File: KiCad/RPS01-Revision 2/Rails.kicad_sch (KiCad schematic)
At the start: 91 parts, among them J200 Power In, J201 Power Out, J202 Header Pins, Q200 BSC009NE2LS5IATMA1 A (TG2)(1A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, Q201 BSC009NE2LS5IATMA1 D (TG1)(2B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, Q202 BSC009NE2LS5IATMA1 C (BG1)(2A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, Q203 BSC009NE2LS5IATMA1 B (BG2)(1B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, U11 LM340MPX-5.0/NOPB, U200 LTC3780EUH-TRPBF, U21 LM340MPX-5.0/NOPB

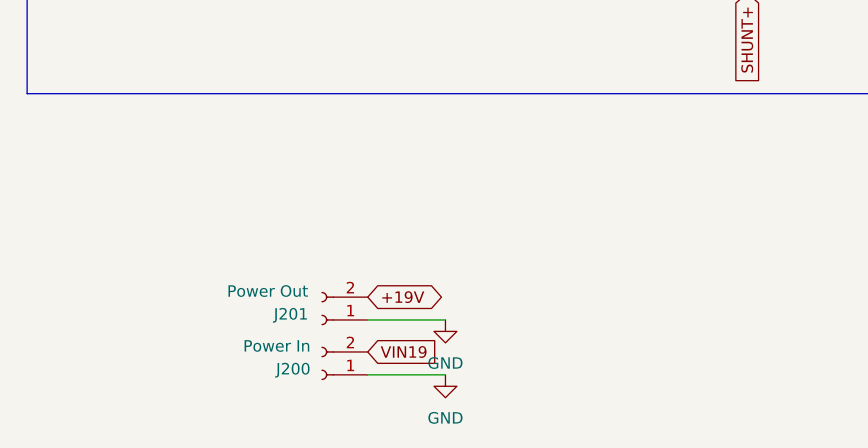
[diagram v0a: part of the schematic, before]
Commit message: Updated some MCU
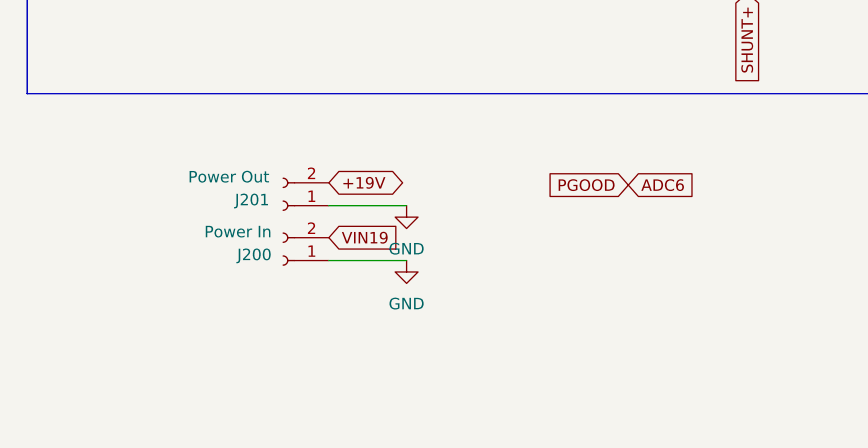
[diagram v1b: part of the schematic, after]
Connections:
- net PGOOD renamed ADC6
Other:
- moved on the sheet: J200, J201
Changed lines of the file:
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@@
     (stroke (width 0) (type default))
   )
-  (wire (pts (xy 289.306 390.906) (xy 297.942 390.906))
+  (wire (pts (xy 284.988 378.206) (xy 293.624 378.206))
     (stroke (width 0) (type default))
   )
@@
     (stroke (width 0) (type default))
   )
-  (wire (pts (xy 289.306 384.81) (xy 297.942 384.81))
+  (wire (pts (xy 284.988 372.11) (xy 293.624 372.11))
     (stroke (width 0) (type default))
   )
@@
     )
   )
-  (global_label "VIN19" (shape input) (at 289.306 388.366 0) (fields_autoplaced)
+  (global_label "VIN19" (shape input) (at 284.988 375.666 0) (fields_autoplaced)
     (effects (font (size 1.27 1.27)) (justify left))
-    (property "Intersheetrefs" "${INTERSHEET_REFS}" (at 297.6547 388.366 0)
+    (property "Intersheetrefs" "${INTERSHEET_REFS}" (at 293.3367 375.666 0)
       (effects (font (size 1.27 1.27)) (justify left) hide)
     )
@@
     )
   )
+  (global_label "PGOOD" (shape input) (at 318.262 369.824 180) (fields_autoplaced)
+    (effects (font (size 1.27 1.27)) (justify right))
+    (property "Intersheetrefs" "${INTERSHEET_REFS}" (at 308.8852 369.824 0)
+      (effects (font (size 1.27 1.27)) (justify right) hide)
+    )
+  )
   (global_label "BOOST2" (shape input) (at 429.514 330.708 180) (fields_autoplaced)
     (effects (font (size 1.27 1.27)) (justify right))
@@
     )
   )
+  (global_label "ADC6" (shape input) (at 318.262 369.824 0) (fields_autoplaced)
+    (effects (font (size 1.27 1.27)) (justify left))
+    (property "Intersheetrefs" "${INTERSHEET_REFS}" (at 326.0059 369.824 0)
+      (effects (font (size 1.27 1.27)) (justify left) hide)
+    )
+  )
   (global_label "VOS+" (shape input) (at 518.922 218.694 180) (fields_autoplaced)
     (effects (font (size 1.27 1.27)) (justify right))
@@
     )
   )
-  (global_label "+19V" (shape bidirectional) (at 289.306 382.27 0) (fields_autoplaced)
+  (global_label "+19V" (shape bidirectional) (at 284.988 369.57 0) (fields_autoplaced)
     (effects (font (size 1.27 1.27)) (justify left))
-    (property "Intersheetrefs" "${INTERSHEET_REFS}" (at 298.4031 382.27 0)
+    (property "Intersheetrefs" "${INTERSHEET_REFS}" (at 294.0851 369.57 0)
       (effects (font (size 1.27 1.27)) (justify left) hide)
     )
@@
     )
   )
-  (symbol (lib_id "power:GND") (at 297.942 390.906 0) (unit 1)
+  (symbol (lib_id "power:GND") (at 293.624 378.206 0) (unit 1)
     (in_bom yes) (on_board yes) (dnp no) (fields_autoplaced)
-    (property "Reference" "#PWR0112" (at 297.942 397.256 0)
+    (property "Reference" "#PWR0112" (at 293.624 384.556 0)
       (effects (font (size 1.27 1.27)) hide)
     )
-    (property "Value" "GND" (at 297.942 395.732 0)
+    (property "Value" "GND" (at 293.624 383.032 0)
       (effects (font (size 1.27 1.27)))
     )
-    (property "Footprint" "" (at 297.942 390.906 0)
+    (property "Footprint" "" (at 293.624 378.206 0)
       (effects (font (size 1.27 1.27)) hide)
     )
-    (property "Datasheet" "" (at 297.942 390.906 0)
+    (property "Datasheet" "" (at 293.624 378.206 0)
       (effects (font (size 1.27 1.27)) hide)
     )
@@
     )
   )
-  (symbol (lib_id "power:GND") (at 297.942 384.81 0) (unit 1)
+  (symbol (lib_id "power:GND") (at 293.624 372.11 0) (unit 1)
     (in_bom yes) (on_board yes) (dnp no) (fields_autoplaced)
-    (property "Reference" "#PWR0111" (at 297.942 391.16 0)
+    (property "Reference" "#PWR0111" (at 293.624 378.46 0)
       (effects (font (size 1.27 1.27)) hide)
     )
-    (property "Value" "GND" (at 297.942 389.636 0)
+    (property "Value" "GND" (at 293.624 376.936 0)
       (effects (font (size 1.27 1.27)))
     )
-    (property "Footprint" "" (at 297.942 384.81 0)
+    (property "Footprint" "" (at 293.624 372.11 0)
       (effects (font (size 1.27 1.27)) hide)
     )
-    (property "Datasheet" "" (at 297.942 384.81 0)
+    (property "Datasheet" "" (at 293.624 372.11 0)
       (effects (font (size 1.27 1.27)) hide)
     )
@@
     )
   )
-  (symbol (lib_id "Connector:Conn_01x02_Socket") (at 284.226 390.906 180) (unit 1)
+  (symbol (lib_id "Connector:Conn_01x02_Socket") (at 279.908 378.206 180) (unit 1)
     (in_bom yes) (on_board yes) (dnp no) (fields_autoplaced)
-    (property "Reference" "J200" (at 282.956 390.271 0)
+    (property "Reference" "J200" (at 278.638 377.571 0)
       (effects (font (size 1.27 1.27)) (justify left))
     )
-    (property "Value" "Power In" (at 282.956 387.731 0)
+    (property "Value" "Power In" (at 278.638 375.031 0)
       (effects (font (size 1.27 1.27)) (justify left))
     )
-    (property "Footprint" "Connector_AMASS:AMASS_XT30U-M_1x02_P5.0mm_Vertical" (at 284.226 390.906 0)
+    (property "Footprint" "Connector_AMASS:AMASS_XT30U-M_1x02_P5.0mm_Vertical" (at 279.908 378.206 0)
       (effects (font (size 1.27 1.27)) hide)
     )
-    (property "Datasheet" "~" (at 284.226 390.906 0)
+    (property "Datasheet" "~" (at 279.908 378.206 0)
       (effects (font (size 1.27 1.27)) hide)
     )
@@
     )
   )
-  (symbol (lib_id "Connector:Conn_01x02_Socket") (at 284.226 384.81 180) (unit 1)
+  (symbol (lib_id "Connector:Conn_01x02_Socket") (at 279.908 372.11 180) (unit 1)
     (in_bom yes) (on_board yes) (dnp no) (fields_autoplaced)
-    (property "Reference" "J201" (at 282.702 384.175 0)
+    (property "Reference" "J201" (at 278.384 371.475 0)
       (effects (font (size 1.27 1.27)) (justify left))
     )
-    (property "Value" "Power Out" (at 282.702 381.635 0)
+    (property "Value" "Power Out" (at 278.384 368.935 0)
       (effects (font (size 1.27 1.27)) (justify left))
     )
-    (property "Footprint" "Connector_AMASS:AMASS_XT30U-F_1x02_P5.0mm_Vertical" (at 284.226 384.81 0)
+    (property "Footprint" "Connector_AMASS:AMASS_XT30U-F_1x02_P5.0mm_Vertical" (at 279.908 372.11 0)
       (effects (font (size 1.27 1.27)) hide)
     )
-    (property "Datasheet" "~" (at 284.226 384.81 0)
+    (property "Datasheet" "~" (at 279.908 372.11 0)
       (effects (font (size 1.27 1.27)) hide)
     )

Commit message: Changed Schematic Refs (pg 2 to 4)
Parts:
- renumbered C216 to C10, C212 to C11, C210 to C12, C200 to C13, C205 to C14, C203 to C15, C218 to C16, C201 to C17, C213 to C18, C215 to C19, C209 to C20, C211 to C21, C214 to C22, C208 to C23, C217 to C24, C207 to C25, C202 to C7, C204 to C8, C206 to C9, D5 to D1, D205 to D10, D6 to D2, D2 to D3, D1 to D4, D204 to D5, D200 to D6, D203 to D7, D201 to D8, D202 to D9, J202 to J13, J201 to J14, J200 to J15, L200 to L2, Q200 to Q1, Q203 to Q2, Q201 to Q3, Q202 to Q4, R208 to R10, R205 to R11, R202 to R12, R204 to R13, R203 to R14, R213 to R15, R201 to R16, R210 to R17, R200 to R18, R214 to R19, R209 to R20, R211 to R21, R207 to R22, R206 to R23, R212 to R9, U21 to U12, U11 to U13, U200 to U16

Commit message: Reduced the References for Peter
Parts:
- renumbered C7 to C15, C8 to C16, C9 to C19, C10 to C20, C11 to C22, C12 to C23, C13 to C24, C14 to C25, C15 to C26, C16 to C27, C17 to C28, C18 to C29, C19 to C32, C20 to C33, C21 to C34, C22 to C35, C23 to C36, C24 to C37, C25 to C38, D9 to D10, D10 to D11, D6 to D7, D7 to D8, D8 to D9, F_3LOGIC1 to F1, F_5LOGIC1 to F2, F_5VB1 to F3, F_12VB1 to F4, R9 to R11, R10 to R12, R11 to R13, R12 to R14, R13 to R15, R14 to R17, R15 to R18, R16 to R19, R17 to R20, R18 to R21, R3_5VB1 to R23, R4_5VB1 to R24, R19 to R25, R20 to R26, R21 to R27, R22 to R28, R23 to R31, R3_12VB1 to R32, R4_12VB1 to R33

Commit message: Completed Schematic
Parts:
- removed J14: Power Out, Connector_AMASS:AMASS_XT30U-F_1x02_P5.0mm_Vertical, symbol Connector:Conn_01x02_Socket
- removed J15: Power In, Connector_AMASS:AMASS_XT30U-M_1x02_P5.0mm_Vertical, symbol Connector:Conn_01x02_Socket
- added F5: 5, Mechatronics Fuses:0154Series_LTF, symbol Device:Fuse_Small
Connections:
- net +19V: now also F5.2; no longer C34.2, C36.2, C38.2, R31.1
- new net: C34.2, C36.2, C38.2, F5.1, R31.1

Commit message: Updates
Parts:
- D7: value B0540W -> S_DIODE_10A; footprint Mechatronic Footprints:CR_SMA_320-340AE_DIO -> Diode_SMD:D_PowerDI-5
- D8: value 1N5819HW -> S_DIODE_10A; footprint Mechatronic Footprints:CR_SMA_320-340AE_DIO -> Diode_SMD:D_PowerDI-5
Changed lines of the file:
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@@
       (effects (font (size 1.27 1.27)) (justify left))
     )
-    (property "Value" "B0540W" (at 317.246 338.074 90)
-      (effects (font (size 1.27 1.27)) (justify left))
-    )
-    (property "Footprint" "Mechatronic Footprints:CR_SMA_320-340AE_DIO" (at 327.152 339.598 0)
+    (property "Value" "S_DIODE_10A" (at 312.42 339.852 90)
+      (effects (font (size 1.27 1.27)) (justify left))
+    )
+    (property "Footprint" "Diode_SMD:D_PowerDI-5" (at 327.152 339.598 0)
       (effects (font (size 1.27 1.27)) hide)
     )
@@
       (effects (font (size 1.27 1.27)))
     )
-    (property "Value" "1N5819HW" (at 343.408 307.848 0)
-      (effects (font (size 1.27 1.27)))
-    )
-    (property "Footprint" "Mechatronic Footprints:CR_SMA_320-340AE_DIO" (at 341.63 310.388 0)
-      (effects (font (size 1.27 1.27)) hide)
-    )
+    (property "Value" "S_DIODE_10A" (at 345.694 313.944 0)
+      (effects (font (size 1.27 1.27)))
+    )
+    (property "Footprint" "Diode_SMD:D_PowerDI-5" (at 341.63 310.388 0)
+      (effects (font (size 1.27 1.27)) hide)
+    )

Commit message: Update
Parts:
- removed R28: 10, Resistor_SMD:R_1206_3216Metric_Pad1.30x1.75mm_HandSolder, symbol Device:R_Small_US
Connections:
- net VIN19 is gone; now on net +BATT2: C24.2, C26.2, C28.2, C35.1, J13.2 (Pin_2), Q1.5, Q1.6, Q1.7, Q1.8, R12.1
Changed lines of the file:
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@@
     (stroke (width 0) (type default))
   )
-  (wire (pts (xy 458.47 215.138) (xy 463.55 215.138))
-    (stroke (width 0) (type default))
-  )
   (wire (pts (xy 292.862 228.092) (xy 294.386 228.092))
     (stroke (width 0) (type default))
@@
     (stroke (width 0) (type default))
   )
-  (wire (pts (xy 468.63 215.138) (xy 471.932 215.138))
+  (wire (pts (xy 458.47 215.138) (xy 471.932 215.138))
     (stroke (width 0) (type default))
   )
@@
         )
       )
-    )
-  )
-  (symbol (lib_id "Device:R_Small_US") (at 466.09 215.138 270) (unit 1)
-    (in_bom yes) (on_board yes) (dnp no)
-    (property "Reference" "R28" (at 466.344 218.186 90)
-      (effects (font (size 1.27 1.27)))
-    )
-    (property "Value" "10" (at 466.471 220.599 90)
-      (effects (font (size 1.27 1.27)))
-    )
-    (property "Footprint" "Resistor_SMD:R_1206_3216Metric_Pad1.30x1.75mm_HandSolder" (at 466.09 215.138 0)
-      (effects (font (size 1.27 1.27)) hide)
-    )
-    (property "Datasheet" "~" (at 466.09 215.138 0)
-      (effects (font (size 1.27 1.27)) hide)
-    )
-    (pin "1")
-    (pin "2")
-    (instances
-      (project "rps01"
-        (path "/14930f15-c0a0-4b55-93e6-b112548415f6/6ed54b0f-f89c-4a82-b1ab-c92c0c126d05"
-          (reference "R28") (unit 1)
-        )
-      )
-      (project "KENESP32LTC370TEST"
-        (path "/5e9cfb74-656a-48c0-8f94-6c53cb1501bf"
-          (reference "R207") (unit 1)
-        )
-      )

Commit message: Finished PCB
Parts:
- removed J13: Header Pins, Connector_PinHeader_2.54mm:PinHeader_1x10_P2.54mm_Vertical, symbol Connector:Conn_01x10_Pin
- added R28: 10, Resistor_SMD:R_1206_3216Metric_Pad1.30x1.75mm_HandSolder, symbol Device:R_Small_US
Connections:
- net +BATT2: now also R28.1; no longer D11.1 (K), U16.23 (VIN)
- new net VIN19: D11.1 (K), R28.2, U16.23 (VIN)
